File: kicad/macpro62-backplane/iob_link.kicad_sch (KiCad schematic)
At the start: 0 parts

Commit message: Cross-board compatibility audit: interface control doc, CR-BP-1 applied, J2/J3 row-swap pinouts, 15-pin face AUX, fan header removed from backplane, CPU board i226/BT1 cleanup
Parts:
- added #BLK6: STUB_IOB_LINK, symbol MP62:STUB_IOB_LINK
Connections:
- net 3V3_SB: now also #BLK6.10 (3V3_SB)
- net I2C_SYS_SCL: now also #BLK6.4 (I2C_SYS_SCL)
- net I2C_SYS_SDA: now also #BLK6.5 (I2C_SYS_SDA)
- net IOB_HALL_A_N: now also #BLK6.2 (IOB_HALL_A_N)
- net IOB_HALL_B_N: now also #BLK6.3 (IOB_HALL_B_N)
- net PWRBTN_IN_N: now also #BLK6.1 (PWRBTN_IN_N)
- new net IOB_INT_N: #BLK6.6 (IOB_INT_N)
- new net IOB_PRSNT_N: #BLK6.7 (IOB_PRSNT_N)
- new net IOB_USB_DN: #BLK6.9 (IOB_USB_DN)
- new net IOB_USB_DP: #BLK6.8 (IOB_USB_DP)
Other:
- note added: "- 1,2 3V3_SB (BP -> IOB) | 3,7,12,15 GND | 4 PWRBTN_IN_N | 5 HALL_A_N | 6 HALL_B_N | 8 I2C_SYS_SCL | 9 I2C_SYS_SDA"
- note added: "- 10 IOB_INT_N (OD, IOB -> BP, BP pull-up) | 11 IOB_PRSNT_N (IOB ties to GND; BP 10k pull-up to 3V3_SB) | 13/14 USB2_LINK D+/D- (CPU-LINK USB2_SPARE)"
- note added: "- IOB high-speed (USB3 x10, DDI, 2x i226 PCIe, VBAT) runs CB J3 -> IOB HS1 directly; 12 V via the IOB 12P PSU header, not the BP"
- note added: "- J6 JST GH 15P (BM15B vertical) <-> IOB J6, 1:1 GH 15P cable (ICD 2026-10-02, pinout = IOB plan 5.3):"
- note removed: "- 3V3_SB supply for the IOB Hall sensors and button; no high-speed signals on this link"
- note removed: "- IOB high-speed (USB3, DP/HDMI, MDI, audio USB) runs CPU board -> IOB directly (TBD with IOB design)"
- note removed: "- J6 JST GH 15P to the new I/O board (designed later): power button, dual Hall interlock, LED/illumination I2C"
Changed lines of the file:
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@@
 	(title_block
 		(title "MP62 backplane: I/O board low-speed link")
-		(date "2026-10-01")
-		(rev "A-bd1")
-		(comment 1 "Block stub: hierarchical labels only, circuit TBD")
+		(date "2026-10-02")
+		(rev "A-bd2")
+		(comment 1 "Block stub: hierarchical labels + one non-BOM stub symbol (#BLKn, passive pins) so ERC sees the nets; circuit TBD")
 	)
 	(hierarchical_label "PWRBTN_IN_N"
@@
 		(effects (font (size 1.27 1.27)) (justify right))
 	)
+	(hierarchical_label "IOB_INT_N"
+		(shape output)
+		(at 38.1 43.18 180)
+		(effects (font (size 1.27 1.27)) (justify right))
+	)
+	(hierarchical_label "IOB_PRSNT_N"
+		(shape output)
+		(at 38.1 45.72 180)
+		(effects (font (size 1.27 1.27)) (justify right))
+	)
+	(hierarchical_label "IOB_USB_DP"
+		(shape bidirectional)
+		(at 38.1 48.26 180)
+		(effects (font (size 1.27 1.27)) (justify right))
+	)
+	(hierarchical_label "IOB_USB_DN"
+		(shape bidirectional)
+		(at 38.1 50.80 180)
+		(effects (font (size 1.27 1.27)) (justify right))
+	)
 	(hierarchical_label "3V3_SB"
 		(shape input)
-		(at 38.1 43.18 180)
+		(at 38.1 53.34 180)
 		(effects (font (size 1.27 1.27)) (justify right))
+	)
+	(symbol
+		(lib_id "MP62:STUB_IOB_LINK")
+		(at 38.1 30.48 0)
+		(unit 1)
+		(exclude_from_sim yes)
+		(in_bom no)
+		(on_board no)
+		(dnp no)
+		(property "Reference" "#BLK6"
+			(at 40.64 27.94 0)
+			(effects (font (size 1.27 1.27)) (justify left) (hide yes))
+		)
+		(property "Value" "STUB_IOB_LINK"
+			(at 40.64 26.67 0)
+			(effects (font (size 1.27 1.27)) (justify left) (hide yes))
+		)
+		(pin "1"
+		)
+		(pin "2"
+		)
+		(pin "3"
+		)
+		(pin "4"
+		)
+		(pin "5"
+		)
+		(pin "6"
+		)
+		(pin "7"
+		)
+		(pin "8"
+		)
+		(pin "9"
+		)
+		(pin "10"
+		)
+		(instances
+			(project "backplane"
+				(path "/6a1c2d3e-0000-4000-8000-000000000062/d310270f-1d7a-44ba-a7bf-682dd6751172"
+					(reference "#BLK6")
+					(unit 1)
+				)
+			)
+		)
 	)
 	(text "BLOCK STUB (rev A block diagram). Contents planned:"
@@
 		(effects (font (size 1.5 1.5)) (justify left bottom))
 	)
-	(text "- J6 JST GH 15P to the new I/O board (designed later): power button, dual Hall interlock, LED/illumination I2C"
+	(text "- J6 JST GH 15P (BM15B vertical) <-> IOB J6, 1:1 GH 15P cable (ICD 2026-10-02, pinout = IOB plan 5.3):"
 		(exclude_from_sim no)
 		(at 76.20 35.56 0)
 		(effects (font (size 1.27 1.27)) (justify left bottom))
 	)
-	(text "- 3V3_SB supply for the IOB Hall sensors and button; no high-speed signals on this link"
+	(text "- 1,2 3V3_SB (BP -> IOB) | 3,7,12,15 GND | 4 PWRBTN_IN_N | 5 HALL_A_N | 6 HALL_B_N | 8 I2C_SYS_SCL | 9 I2C_SYS_SDA"
 		(exclude_from_sim no)
 		(at 76.20 39.37 0)
 		(effects (font (size 1.27 1.27)) (justify left bottom))
 	)
-	(text "- IOB high-speed (USB3, DP/HDMI, MDI, audio USB) runs CPU board -> IOB directly (TBD with IOB design)"
+	(text "- 10 IOB_INT_N (OD, IOB -> BP, BP pull-up) | 11 IOB_PRSNT_N (IOB ties to GND; BP 10k pull-up to 3V3_SB) | 13/14 USB2_LINK D+/D- (CPU-LINK USB2_SPARE)"
 		(exclude_from_sim no)
 		(at 76.20 43.18 0)
 		(effects (font (size 1.27 1.27)) (justify left bottom))
 	)
+	(text "- IOB high-speed (USB3 x10, DDI, 2x i226 PCIe, VBAT) runs CB J3 -> IOB HS1 directly; 12 V via the IOB 12P PSU header, not the BP"
+		(exclude_from_sim no)
+		(at 76.20 46.99 0)
+		(effects (font (size 1.27 1.27)) (justify left bottom))
+	)

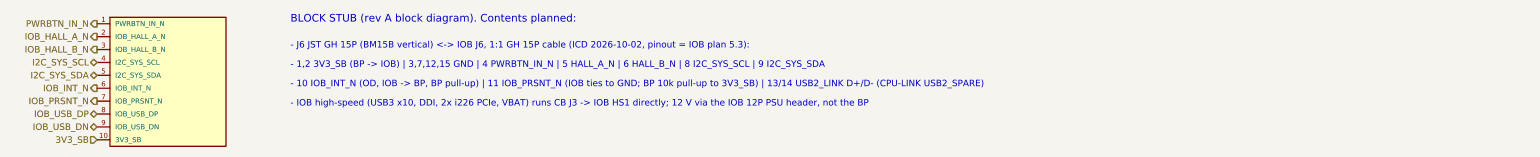
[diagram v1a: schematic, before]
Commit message: ICD rev 2: 45 deg faces, 445 W ceiling + live power target (INA228 telemetry), ribbon MCIO jog cables, BT on S0, fan fail-safe, port-module I2C map
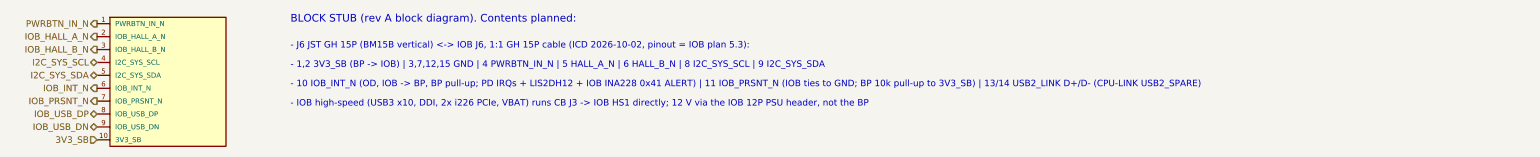
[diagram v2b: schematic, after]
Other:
- note added: "- 10 IOB_INT_N (OD, IOB -> BP, BP pull-up; PD IRQs + LIS2DH12 + IOB INA228 0x41 ALERT) | 11 IOB_PRSNT_N (IOB ties to GND; BP 10k pull-up to 3V3_SB) | 13/14 USB2_LINK D+/D- (CPU-LINK USB2_SPARE)"
- note removed: "- 10 IOB_INT_N (OD, IOB -> BP, BP pull-up) | 11 IOB_PRSNT_N (IOB ties to GND; BP 10k pull-up to 3V3_SB) | 13/14 USB2_LINK D+/D- (CPU-LINK USB2_SPARE)"
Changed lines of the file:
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@@
 		(instances
 			(project "backplane"
-				(path "/6a1c2d3e-0000-4000-8000-000000000062/d310270f-1d7a-44ba-a7bf-682dd6751172"
+				(path "/6a1c2d3e-0000-4000-8000-000000000062/d2853bf2-9194-4765-a7f9-2878ed84dcbe"
 					(reference "#BLK6")
 					(unit 1)
@@
 		(effects (font (size 1.27 1.27)) (justify left bottom))
 	)
-	(text "- 10 IOB_INT_N (OD, IOB -> BP, BP pull-up) | 11 IOB_PRSNT_N (IOB ties to GND; BP 10k pull-up to 3V3_SB) | 13/14 USB2_LINK D+/D- (CPU-LINK USB2_SPARE)"
+	(text "- 10 IOB_INT_N (OD, IOB -> BP, BP pull-up; PD IRQs + LIS2DH12 + IOB INA228 0x41 ALERT) | 11 IOB_PRSNT_N (IOB ties to GND; BP 10k pull-up to 3V3_SB) | 13/14 USB2_LINK D+/D- (CPU-LINK USB2_SPARE)"
 		(exclude_from_sim no)
 		(at 76.20 43.18 0)
